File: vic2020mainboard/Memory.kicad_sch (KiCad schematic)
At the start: 4 parts, among them J1 A15 KERNAL/BASIC SELECT, J2 A14 Kernel/Basic Select, U12 AS6C1008-55PCN, U13 27512

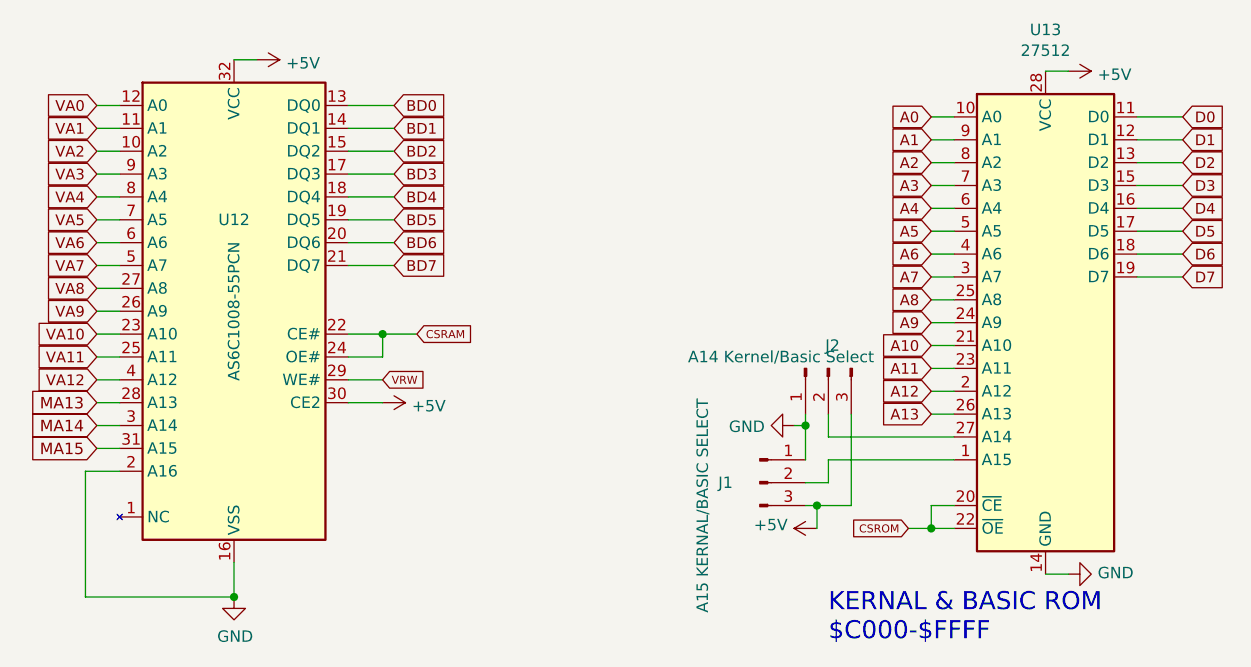
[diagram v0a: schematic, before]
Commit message: Added power supply circuit for 9V AC input
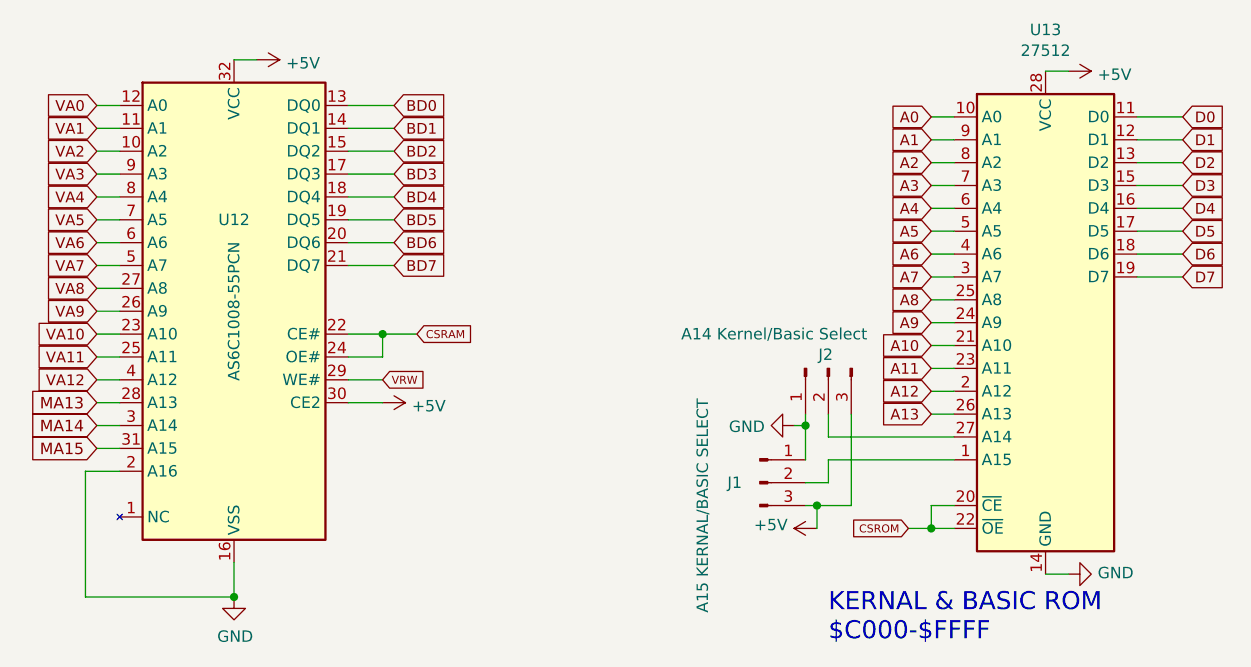
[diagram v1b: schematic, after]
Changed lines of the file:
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@@
 		(dnp no)
 		(property "Reference" "J2"
-			(at 135.89 80.01 90)
+			(at 135.128 81.026 90)
 			(show_name no)
 			(do_not_autoplace no)
@@
 		)
 		(property "Value" "A14 Kernel/Basic Select"
-			(at 139.7 81.28 90)
+			(at 138.938 78.74 90)
 			(show_name no)
 			(do_not_autoplace no)
@@
 		(dnp no)
 		(property "Reference" "J1"
-			(at 123.19 95.25 0)
-			(show_name no)
-			(do_not_autoplace no)
+			(at 124.206 95.25 0)
+			(show_name no)
+			(do_not_autoplace no)
